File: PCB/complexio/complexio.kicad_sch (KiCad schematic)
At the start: 24 parts, among them J1 Bluetooth HC-05 module, SW1 SW_SPDT, U1 STM32F103C8T6, U10 KTIR0711S, U11 KTIR0711S, U2 TB6612FNG, U3 TB6612FNG, U4 KTIR0711S, U5 KTIR0711S, U6 KTIR0711S, U7 KTIR0711S, U8 KTIR0711S, U9 KTIR0711S

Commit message: Initial code,schem & added assets
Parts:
- removed U10, U11, U4, U5, U6, U7, U8, U9: KTIR0711S, symbol KTIR0711S:KTIR0711S
- added IMU1: MPU6050, MPU6050:MPU6050, symbol MPU6050:MPU6050
- added OLED1: SPI OLED Screen 128x64 pixels, Connector_PinSocket_2.54mm:PinSocket_1x07_P2.54mm_Vertical, symbol Connector:Conn_01x07_Socket
- added SWD1: Serial Wire Debug Interface connector, symbol Connector:Conn_01x04_Pin
- BL1: renamed from J1; JLCPCB Part # (none) -> C40877; MFR.Part # (none) -> 2.54-1*6PFemale; Manufacturer (none) -> BOOMELE(Boom Precision Elec); Package (none) -> Plugin,P=2.54mm
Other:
- added sheet Sensor_array (Sensor_array.kicad_sch)
- moved on the sheet: BL1, U2, U3

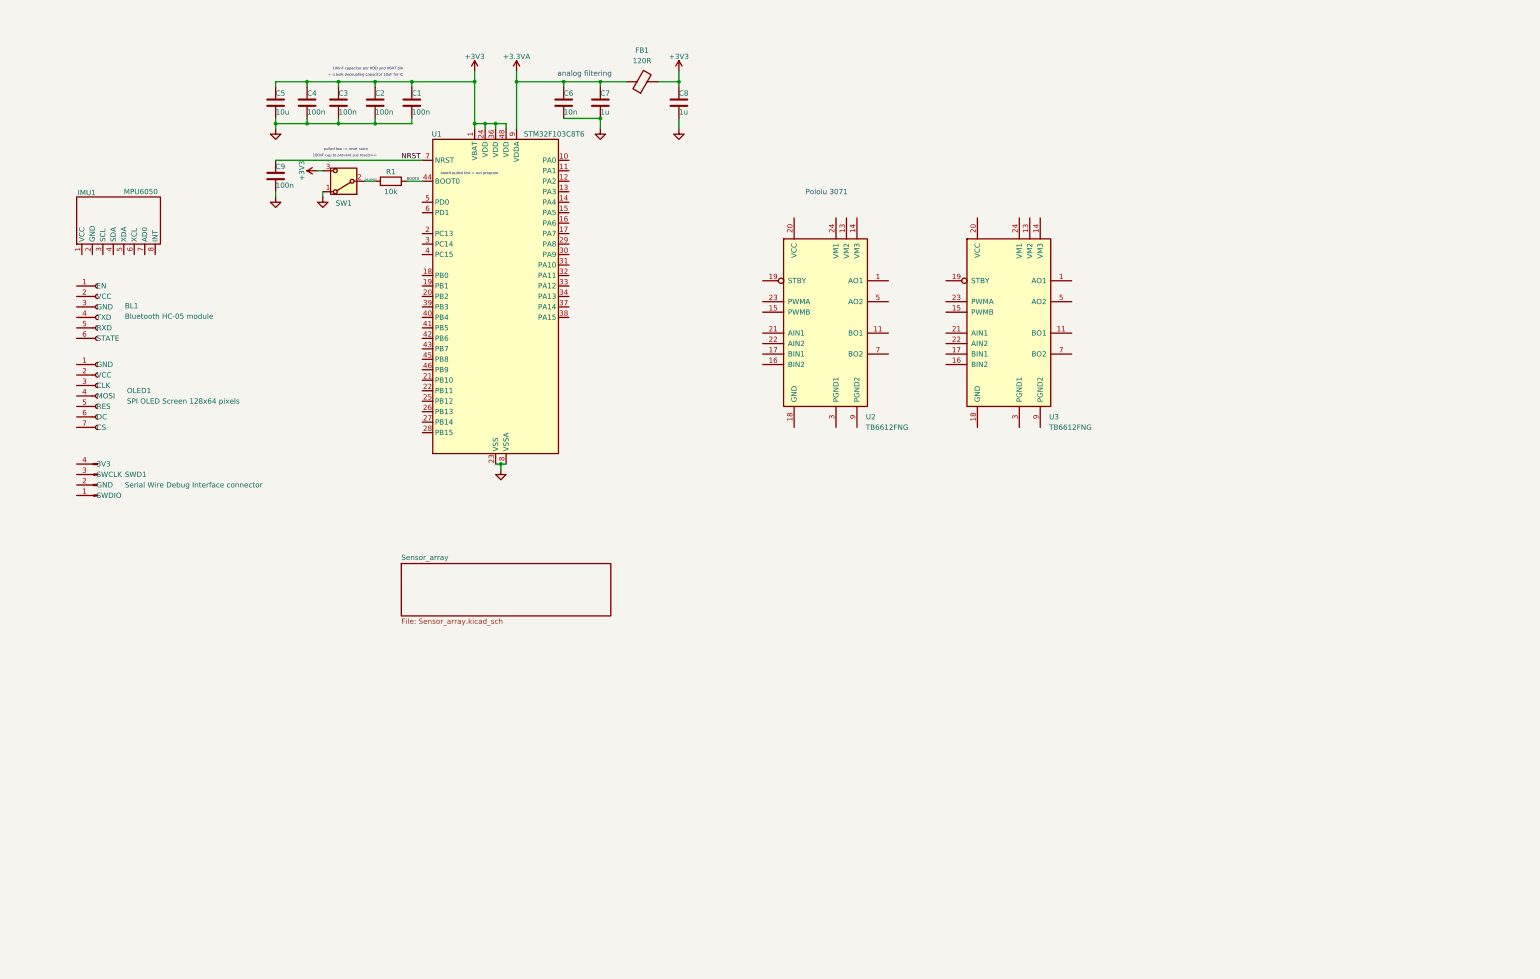
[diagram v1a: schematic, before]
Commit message: Sensor array finished & main schem modified
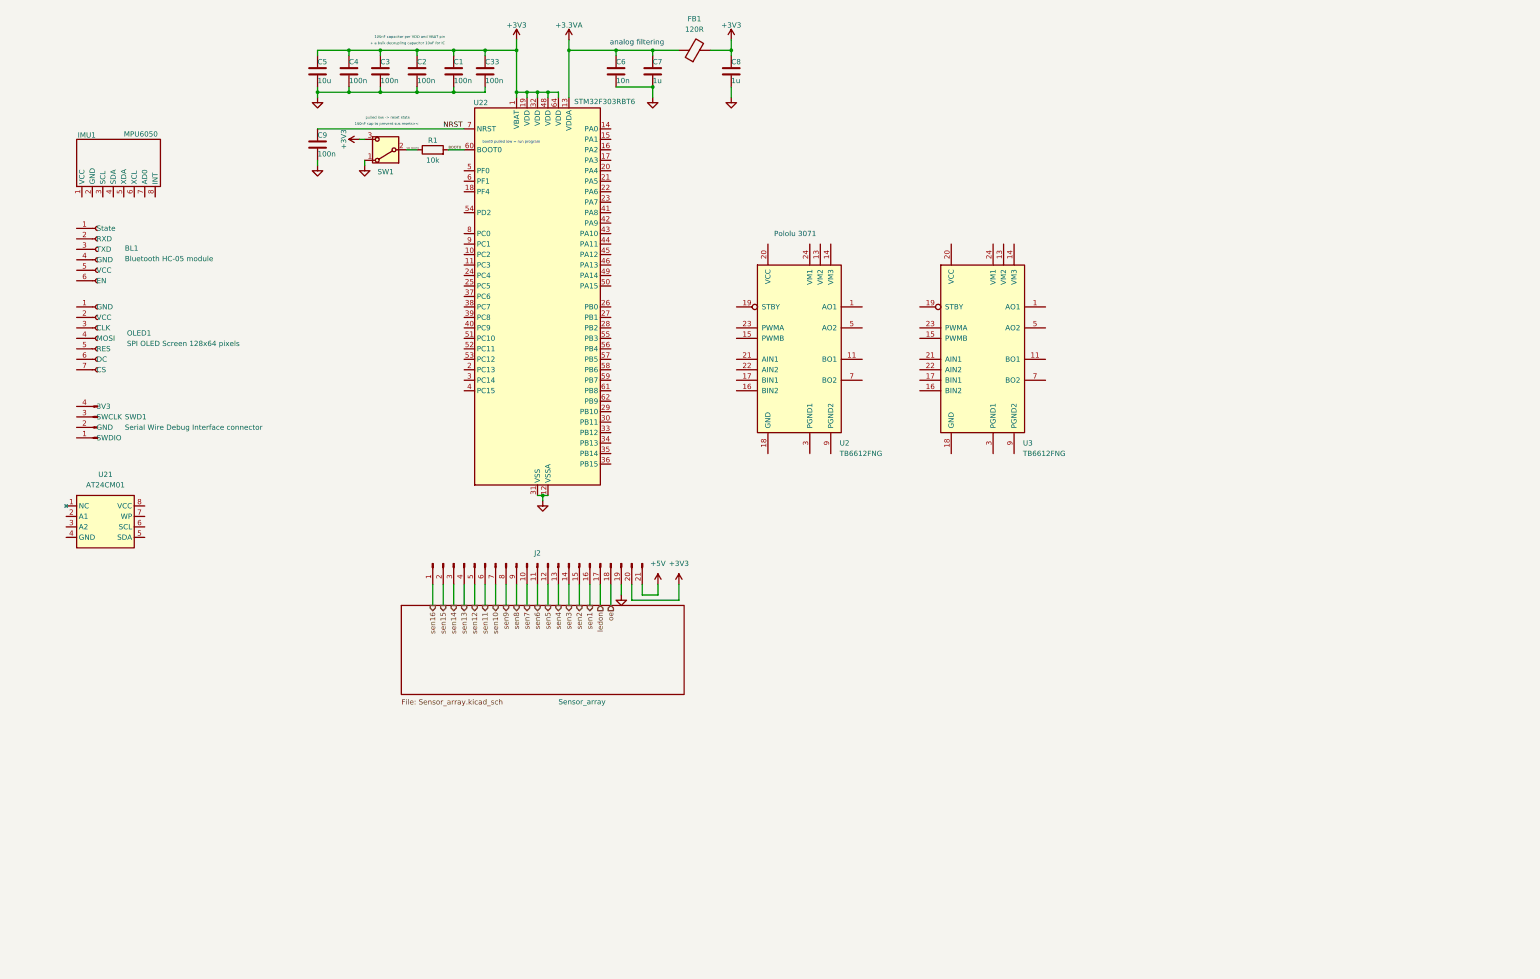
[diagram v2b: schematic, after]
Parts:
- removed U1: STM32F103C8T6, Package_QFP:LQFP-48_7x7mm_P0.5mm, symbol MCU_ST_STM32F1:STM32F103C8Tx
- added C33: 100n, Capacitor_SMD:C_0402_1005Metric, symbol Device:C
- added J2: Conn_01x21_Pin, Connector_PinHeader_1.27mm:PinHeader_1x21_P1.27mm_Horizontal, symbol Connector:Conn_01x21_Pin
- added U21: AT24CM01, AT24CM01:AT24CM01, symbol AT24CM01:AT24CM01
- added U22: STM32F303RBT6, Package_QFP:LQFP-64_10x10mm_P0.5mm, symbol MCU_ST_STM32F3:STM32F303RBTx
- BL1: footprint Connector_PinSocket_2.54mm:PinSocket_1x06_P2.54mm_Vertical -> Connector_PinSocket_2.54mm:PinSocket_1x07_P2.54mm_Horizontal
- SWD1: footprint (none) -> Connector_PinHeader_2.54mm:PinHeader_1x04_P2.54mm_Horizontal; JLCPCB Part # (none) -> C91552; MFR.Part # (none) -> 2.54-1*4P反弯排针; Manufacturer (none) -> BOOMELE(Boom Precision Elec); Package (none) -> Push-Pull,P=2.54mm
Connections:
- net +3.3VA: now also U22.13 (VDDA)
- net +3V3: now also C33.1, J2.20 (Pin_20), U22.1 (VBAT), U22.19 (VDD), U22.32 (VDD), U22.48 (VDD), U22.64 (VDD)
- net BOOT0: now also U22.60 (BOOT0)
- net GND: now also C33.2, J2.19 (Pin_19), U22.12 (VSSA), U22.31 (VSS), U22.47 (VSS), U22.63 (VSS)
- net NRST: now also U22.7 (NRST)
- new net +5V: J2.21 (Pin_21)
- new net ledon: J2.17 (Pin_17)
- new net oe: J2.18 (Pin_18)
- new net sen1: J2.16 (Pin_16)
- new net sen10: J2.7 (Pin_7)
- new net sen11: J2.6 (Pin_6)
- new net sen12: J2.5 (Pin_5)
- new net sen13: J2.4 (Pin_4)
- new net sen14: J2.3 (Pin_3)
- new net sen15: J2.2 (Pin_2)
- new net sen16: J2.1 (Pin_1)
- new net sen2: J2.15 (Pin_15)
- new net sen3: J2.14 (Pin_14)
- new net sen4: J2.13 (Pin_13)
- new net sen5: J2.12 (Pin_12)
- new net sen6: J2.11 (Pin_11)
- new net sen7: J2.10 (Pin_10)
- new net sen8: J2.9 (Pin_9)
- new net sen9: J2.8 (Pin_8)
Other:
- moved on the sheet: BL1, C1, C2, C3, C4, C5, C6, C7, C8, C9, FB1, IMU1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

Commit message: Changed firmware & SMD of mpu6050+minor changes
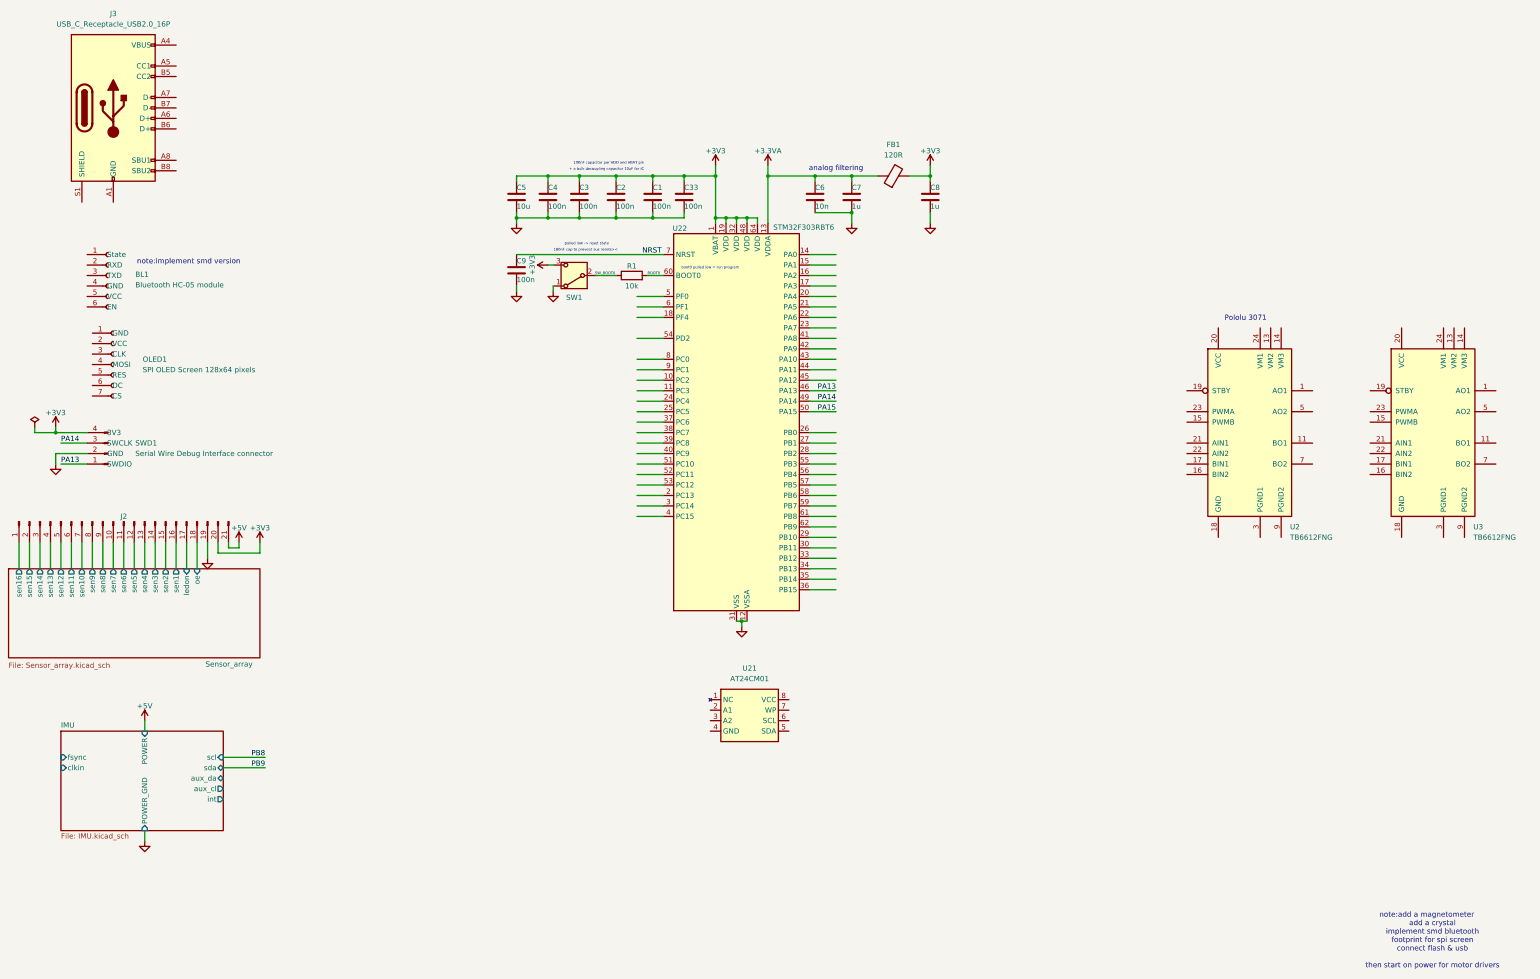
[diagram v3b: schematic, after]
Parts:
- removed IMU1: MPU6050, MPU6050:MPU6050, symbol MPU6050:MPU6050
- added J3: USB_C_Receptacle_USB2.0_16P, Connector_USB:USB_C_Receptacle_GCT_USB4105-xx-A_16P_TopMnt_Horizontal, symbol Connector:USB_C_Receptacle_USB2.0_16P
- U22: Distributor link 1 (none) -> https://eu.mouser.com/ProductDetail/STMicroelectronics/STM3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; Distributor link 2 (none) -> https://www.digikey.com/en/products/detail/stmicroelectroni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; JLCPCB Part # (none) -> C130453; MFR.Part # (none) -> STM32F303RBT6; Manufacturer (none) -> STMicroelectronics; Package (none) -> LQFP-64(10x10)
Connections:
- net +3V3: now also SWD1.4 (3V3)
- net GND: now also SWD1.2 (GND)
- net PA13: now reaches SWD1.1 (SWDIO)
- net PA13: now also U22.46 (PA13)
- net PA14: now reaches SWD1.3 (SWCLK)
- net PA14: now also U22.49 (PA14)
- net PA15: now reaches U22.50 (PA15)
- net ledon renamed Sensor_array/ledon
- net oe renamed Sensor_array/oe
- net sen1 renamed Sensor_array/sen1
- net sen10 renamed Sensor_array/sen10
- net sen11 renamed Sensor_array/sen11
- net sen12 renamed Sensor_array/sen12
- net sen13 renamed Sensor_array/sen13
- net sen14 renamed Sensor_array/sen14
- net sen15 renamed Sensor_array/sen15
- net sen16 renamed Sensor_array/sen16
- net sen2 renamed Sensor_array/sen2
- net sen3 renamed Sensor_array/sen3
- net sen4 renamed Sensor_array/sen4
- net sen5 renamed Sensor_array/sen5
- net sen6 renamed Sensor_array/sen6
- net sen7 renamed Sensor_array/sen7
- net sen8 renamed Sensor_array/sen8
- net sen9 renamed Sensor_array/sen9
- new net: J3.A1 (GND), J3.A12 (GND), J3.B1 (GND), J3.B12 (GND)
- new net: J3.A4 (VBUS), J3.A9 (VBUS), J3.B4 (VBUS), J3.B9 (VBUS)
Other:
- added sheet IMU (IMU.kicad_sch)
- sheet Sensor_array ports: added ledon, oe, sen1, sen10, sen11, sen12, sen13, sen14, sen15, sen16, sen2, sen3, sen4, sen5, sen6, sen7, sen8, sen9; removed none
- note added: "note:add a magnetometer add a crystal implement smd bluetooth footprint for spi screen connect flash & usb then start on power for motor drivers"
- note added: "note:implement smd version"
- moved on the sheet: BL1, C1, C2, C3, C33, C4, C5, C6, C7, C8, C9, FB1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
